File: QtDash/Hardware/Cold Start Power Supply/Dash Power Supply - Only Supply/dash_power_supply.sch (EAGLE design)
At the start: 55 parts, among them IC1 LM5060, IC2 LM3488, Q1 IPB042N10N3GATMA1, Q2 IPB042N10N3GATMA1, Q3 BC816-25HVL, Q4 BSC027N04LSG

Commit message: bugfix/hardware-revA-issues: 	- added supply only board for testing separately and more cheaply 	- added resistor values to cold start board library
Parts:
- removed C1, C17, C2, C4: 0.1u, dash_power_supply:CL32B104KCFNNWE
- removed C16, C3: 4.7u, dash_power_supply:CL32B475KCVZW6E
- removed C5: 100n, digital_dash:CL10B104MB8NNNC
- removed D1, D3: 24V, dash_power_supply:5.0SMDJ24A
- removed D10, D11, D5: NSR0170HT1G, dash_power_supply:NSR0170HT1G
- removed D2: 13V, dash_power_supply:PTVS13VS1UR,115
- removed D4, D6: 200V, dash_power_supply:ES07B-GS18
- removed D7, D8: 24V, dash_power_supply:SZ1SMA24AT3G
- removed IC1: LM5060, dash_power_supply:LM5060
- removed J3: (no value), SparkFun-Connectors:CONN_02PTH4
- removed Q1, Q2: IPB042N10N3GATMA1, dash_power_supply:IPB042N10N3GATMA1
- removed Q3: BC816-25HVL, dash_power_supply:BC816-25HVL
- removed R1: 390k, SparkFun-Resistors:390KOHM-0603-1/10W-1%
- removed R2: 2.0k, SparkFun-Resistors:2.0KOHM-0603-1/10W-5%
- removed R3, R4: 200, SparkFun-Resistors:RESISTOR1206
- removed R5, R6, R9: 10k, SparkFun-Resistors:10KOHM-0603-1/10W-1%
- removed R7: 470k, SparkFun-Resistors:470KOHM
- removed R8: 15k, SparkFun-Resistors:15KOHM-0603-1/10W-1%
- R10: device SparkFun-Resistors:20KOHM-0603-1/10W-5% -> digital_dash:RC0603JR-0720KL
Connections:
- removed net G: D5.A, Q1.G, Q2.G, Q3.C, R2.1
- removed net GATE: D5.C, IC1.GATE, R2.2
- removed net N$10: IC1.OUT, R9.1
- removed net N$2: C1.2, C2.1
- removed net N$23: D11.C, R5.1
- removed net N$3: IC1.EN, R5.2
- removed net N$4: D6.A, R3.1, R4.1
- removed net N$6: D8.C, IC1.SENSE, R6.1
- removed net N$7: D4.C, Q3.B, R1.1
- removed net N$8: IC1.OVP, R7.1, R8.2
- removed net N$9: C5.1, IC1.TIMER
- removed net VIN: C1.1, D1.C, J1.2, Q1.D, R3.2, R4.2, R6.2, R7.2
- removed net VIN_INTERNAL: D1.A, D2.A, D4.A, Q1.S, Q2.S, Q3.E
- removed net VIN_LM5060: C3.1, C4.1, D10.C, D11.A, D6.C, D7.C, IC1.UVLO, IC1.VIN
- net 5V: no longer D10.A
- net GND: no longer C16.2, C17.2, C2.2, C3.2, C4.2, C5.2, D3.A, D7.A, D8.A, IC1.GND, J3.1, R1.2, R8.1
- net VBATT: now also J1.2; no longer C16.1, C17.1, D2.C, D3.C, J3.2, Q2.D, R9.2
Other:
- note removed: "Input Protection"

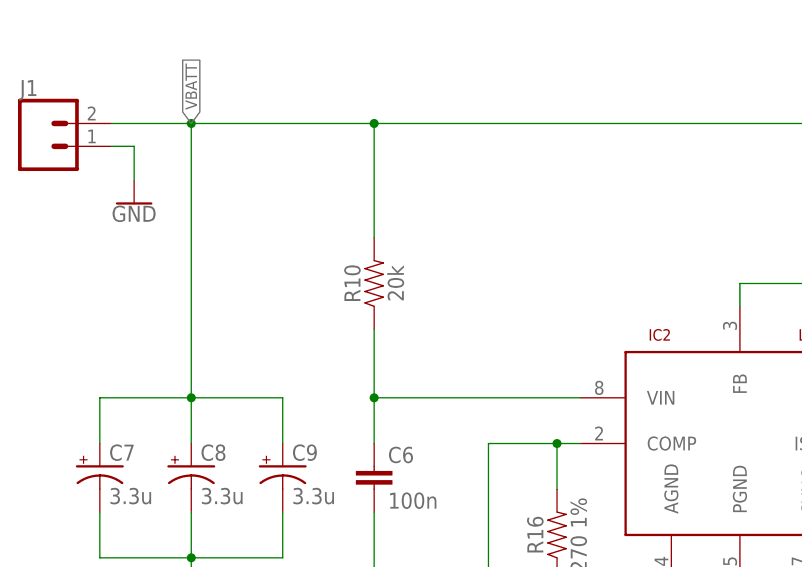
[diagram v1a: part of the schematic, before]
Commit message: topic/component-optimization: 	- 20k resistor on vin of power supply should have been 20R 	- fixed silk screen on cold start power supply 	- re-arranged components a via for cleaner return paths
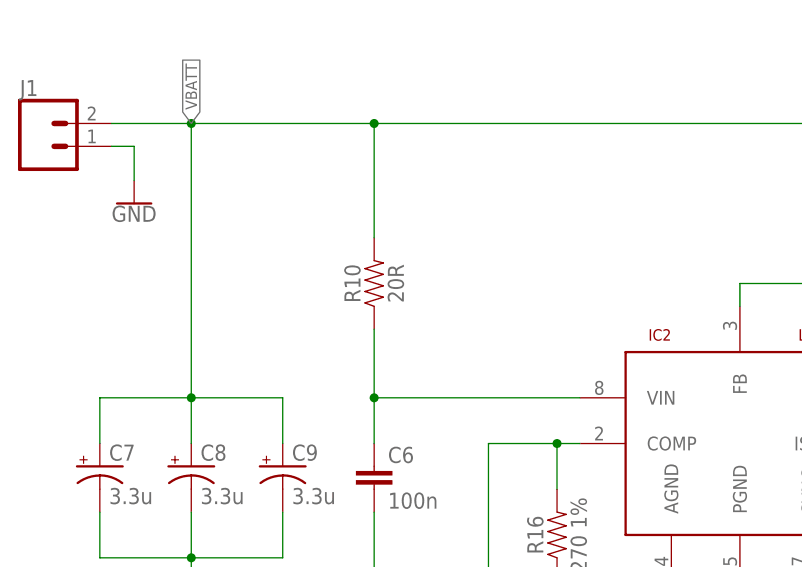
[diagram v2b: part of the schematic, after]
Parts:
- R10: value 20k -> 20R; device digital_dash:RC0603JR-0720KL -> digital_dash:RC0603JR-0720RL
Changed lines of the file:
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@@
 <setting verticaltext="up"/>
 </settings>
-<grid distance="0.05" unitdist="inch" unit="inch" style="lines" multiple="1" display="no" altdistance="0.01" altunitdist="inch" altunit="inch"/>
+<grid distance="0.1" unitdist="inch" unit="inch" style="lines" multiple="1" display="no" altdistance="0.01" altunitdist="inch" altunit="inch"/>
 <layers>
 <layer number="1" name="Top" color="4" fill="1" visible="no" active="no"/>
@@
 <part name="IC2" library="dash_power_supply" deviceset="LM3488" device=""/>
 <part name="C6" library="digital_dash" deviceset="CL" device="" technology="10B104MB8NNNC" value="100n"/>
-<part name="R10" library="digital_dash" deviceset="RC0603JR" device="" technology="-0720KL" value="20k"/>
+<part name="R10" library="digital_dash" deviceset="RC0603JR" device="" technology="-0720RL" value="20R"/>
 <part name="R11" library="digital_dash" deviceset="RC0603JR" device="" technology="-07100RL" value="100R"/>
 <part name="R12" library="dash_power_supply" deviceset="RC1206FR" device="" technology="-0730K9L" value="30.9k 1%"/>

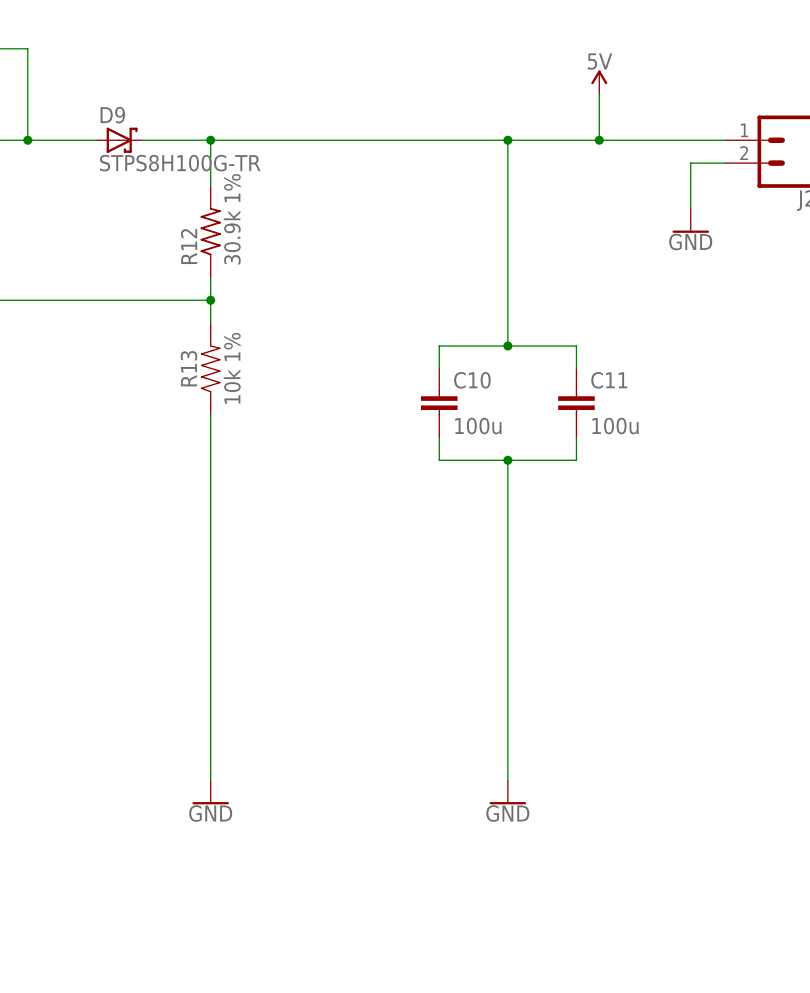
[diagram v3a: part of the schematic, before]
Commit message: topic/component-optimization: 	- added some more output capacitors
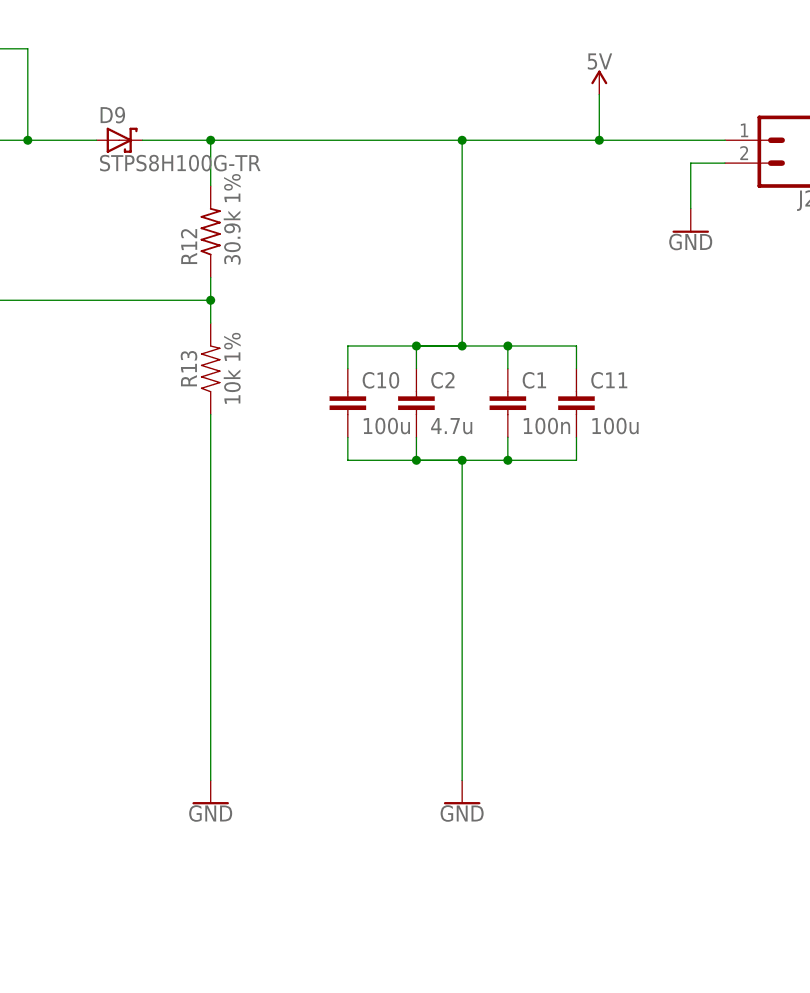
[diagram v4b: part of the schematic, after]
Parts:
- added C1: 100n, digital_dash:CL10B104MB8NNNC
- added C2: 4.7u, digital_dash:CL10A475KL8NRNC
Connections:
- net 5V: now also C1.1, C2.1
- net GND: now also C1.2, C2.2
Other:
- moved on the sheet: C10
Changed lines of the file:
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@@
 <part name="J1" library="SparkFun-Connectors" deviceset="CONN_02" device="PTH4"/>
 <part name="GND1" library="SparkFun-PowerSymbols" deviceset="GND" device=""/>
+<part name="C1" library="digital_dash" deviceset="CL" device="" technology="10B104MB8NNNC" value="100n"/>
+<part name="C2" library="digital_dash" deviceset="CL" device="" technology="10A475KL8NRNC" value="4.7u"/>
 </parts>
 <sheets>
@@
 <instance part="GND13" gate="1" x="165.1" y="86.36"/>
 <instance part="C12" gate="G$1" x="137.16" y="160.02" rot="R90"/>
-<instance part="GND14" gate="1" x="198.12" y="86.36"/>
+<instance part="GND14" gate="1" x="193.04" y="86.36"/>
 <instance part="SUPPLY1" gate="G$1" x="208.28" y="165.1"/>
 <instance part="R17" gate="G$1" x="114.3" y="129.54"/>
@@
 <instance part="C15" gate="G$1" x="114.3" y="106.68"/>
 <instance part="R13" gate="G$1" x="165.1" y="134.62" rot="R90"/>
-<instance part="C10" gate="G$1" x="190.5" y="132.08"/>
+<instance part="C10" gate="G$1" x="180.34" y="132.08"/>
 <instance part="C11" gate="G$1" x="205.74" y="132.08"/>
 <instance part="C7" gate="G$1" x="15.24" y="121.92"/>
@@
 <instance part="J1" gate="G$1" x="8.89" y="157.48"/>
 <instance part="GND1" gate="1" x="19.05" y="151.13"/>
+<instance part="C1" gate="G$1" x="198.12" y="129.54"/>
+<instance part="C2" gate="G$1" x="187.96" y="129.54"/>
 </instances>
 <busses>
@@
 <wire x1="205.74" y1="127" x2="205.74" y2="124.46" width="0.1524" layer="91"/>
 <wire x1="205.74" y1="124.46" x2="198.12" y2="124.46" width="0.1524" layer="91"/>
-<wire x1="198.12" y1="124.46" x2="190.5" y2="124.46" width="0.1524" layer="91"/>
-<wire x1="190.5" y1="124.46" x2="190.5" y2="127" width="0.1524" layer="91"/>
-<wire x1="198.12" y1="124.46" x2="198.12" y2="88.9" width="0.1524" layer="91"/>
-<junction x="198.12" y="124.46"/>
+<wire x1="198.12" y1="124.46" x2="193.04" y2="124.46" width="0.1524" layer="91"/>
+<wire x1="187.96" y1="124.46" x2="193.04" y2="124.46" width="0.1524" layer="91"/>
+<wire x1="193.04" y1="124.46" x2="180.34" y2="124.46" width="0.1524" layer="91"/>
+<wire x1="180.34" y1="124.46" x2="180.34" y2="127" width="0.1524" layer="91"/>
+<wire x1="193.04" y1="124.46" x2="193.04" y2="88.9" width="0.1524" layer="91"/>
+<junction x="193.04" y="124.46"/>
 <pinref part="GND14" gate="1" pin="GND"/>
 <pinref part="C10" gate="G$1" pin="2"/>
 <pinref part="C11" gate="G$1" pin="2"/>
+<pinref part="C2" gate="G$1" pin="2"/>
+<wire x1="187.96" y1="124.46" x2="187.96" y2="127" width="0.1524" layer="91"/>
+<junction x="187.96" y="124.46"/>
+<pinref part="C1" gate="G$1" pin="2"/>
+<wire x1="198.12" y1="124.46" x2="198.12" y2="127" width="0.1524" layer="91"/>
+<junction x="198.12" y="124.46"/>
 </segment>
 <segment>
@@
 <wire x1="205.74" y1="134.62" x2="205.74" y2="137.16" width="0.1524" layer="91"/>
 <wire x1="205.74" y1="137.16" x2="198.12" y2="137.16" width="0.1524" layer="91"/>
-<wire x1="198.12" y1="137.16" x2="190.5" y2="137.16" width="0.1524" layer="91"/>
-<wire x1="190.5" y1="137.16" x2="190.5" y2="134.62" width="0.1524" layer="91"/>
+<wire x1="198.12" y1="137.16" x2="193.04" y2="137.16" width="0.1524" layer="91"/>
+<wire x1="187.96" y1="137.16" x2="193.04" y2="137.16" width="0.1524" layer="91"/>
+<wire x1="193.04" y1="137.16" x2="180.34" y2="137.16" width="0.1524" layer="91"/>
+<wire x1="180.34" y1="137.16" x2="180.34" y2="134.62" width="0.1524" layer="91"/>
 <pinref part="R12" gate="G$1" pin="2"/>
 <wire x1="165.1" y1="160.02" x2="165.1" y2="154.94" width="0.1524" layer="91"/>
 <wire x1="157.48" y1="160.02" x2="165.1" y2="160.02" width="0.1524" layer="91"/>
-<wire x1="198.12" y1="137.16" x2="198.12" y2="160.02" width="0.1524" layer="91"/>
-<wire x1="198.12" y1="160.02" x2="165.1" y2="160.02" width="0.1524" layer="91"/>
-<junction x="198.12" y="137.16"/>
+<wire x1="193.04" y1="137.16" x2="193.04" y2="160.02" width="0.1524" layer="91"/>
+<wire x1="193.04" y1="160.02" x2="165.1" y2="160.02" width="0.1524" layer="91"/>
+<junction x="193.04" y="137.16"/>
 <junction x="165.1" y="160.02"/>
-<wire x1="198.12" y1="160.02" x2="208.28" y2="160.02" width="0.1524" layer="91"/>
+<wire x1="193.04" y1="160.02" x2="208.28" y2="160.02" width="0.1524" layer="91"/>
 <wire x1="208.28" y1="160.02" x2="208.28" y2="165.1" width="0.1524" layer="91"/>
-<junction x="198.12" y="160.02"/>
+<junction x="193.04" y="160.02"/>
 <pinref part="SUPPLY1" gate="G$1" pin="5V"/>
 <pinref part="C10" gate="G$1" pin="1"/>
@@
 <wire x1="208.28" y1="160.02" x2="222.25" y2="160.02" width="0.1524" layer="91"/>
 <junction x="208.28" y="160.02"/>
-</segment>
-</net>
+<pinref part="C1" gate="G$1" pin="1"/>
+<wire x1="198.12" y1="134.62" x2="198.12" y2="137.16" width="0.1524" layer="91"/>
+<junction x="198.12" y="137.16"/>
+<pinref part="C2" gate="G$1" pin="1"/>
+<wire x1="187.96" y1="134.62" x2="187.96" y2="137.16" width="0.1524" layer="91"/>
+<junction x="187.96" y="137.16"/>
+</segment>
+</net>

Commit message: topic/component-optimization: 	- rev b of cold start supply ordered
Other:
- moved on the sheet: C1, C10, C11, C12, C13, C14, C15, C2, C6, C7, C8, C9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

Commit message: 82-bom-missing: 	- added BOM for eagle version of the power supply
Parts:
- Q4: value BSC027N04LSG -> DMTH6002LPS-13; device dash_power_supply:BSC027N04LSG -> dash_power_supply:DMTH6002LPS-13
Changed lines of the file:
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@@
 <part name="SUPPLY1" library="SparkFun-PowerSymbols" deviceset="5V" device=""/>
 <part name="R17" library="SparkFun-Resistors" deviceset="0OHM" device="-0603-1/10W" value="0"/>
-<part name="Q4" library="dash_power_supply" deviceset="BSC027N04LSG" device=""/>
+<part name="Q4" library="dash_power_supply" deviceset="DMTH6002LPS-13" device=""/>
 <part name="C13" library="digital_dash" deviceset="CL" device="" technology="10B684KO8NFNC" value=".68u"/>
 <part name="C14" library="digital_dash" deviceset="CL" device="" technology="10B102KB8NNWC" value="1n"/>
